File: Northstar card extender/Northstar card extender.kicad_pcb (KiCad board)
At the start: 2 copper layers, 76.1 x 36 mm, 17 parts, among them J1 male card edge, J2 female slot pass through, J3 ribbon expansion

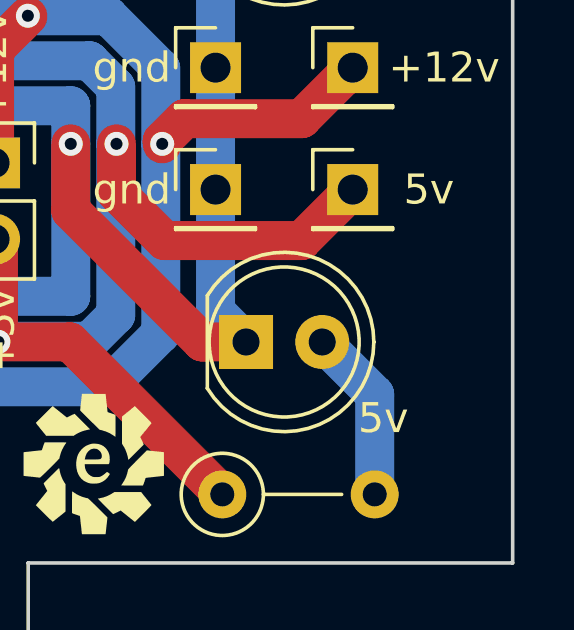
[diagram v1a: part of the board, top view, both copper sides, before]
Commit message: added silkscreen for direction
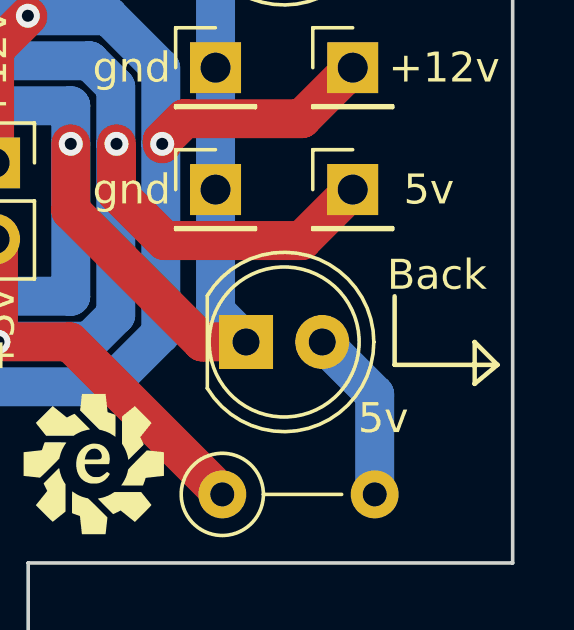
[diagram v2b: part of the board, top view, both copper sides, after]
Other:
- board text added: "Back"
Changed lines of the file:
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@@
       (stroke (width 0) (type solid)) (fill solid) (layer "B.SilkS"))
   )
+  (gr_line (start 173.482 110.744) (end 173.482 112.141)
+    (stroke (width 0.15) (type default)) (layer "F.SilkS"))
+  (gr_line (start 173.482 112.141) (end 174.244 111.506)
+    (stroke (width 0.15) (type default)) (layer "F.SilkS"))
+  (gr_line (start 174.244 111.506) (end 173.482 110.744)
+    (stroke (width 0.15) (type default)) (layer "F.SilkS"))
+  (gr_line (start 170.815 111.506) (end 174.244 111.506)
+    (stroke (width 0.15) (type default)) (layer "F.SilkS"))
+  (gr_line (start 170.815 109.22) (end 170.815 111.506)
+    (stroke (width 0.15) (type default)) (layer "F.SilkS"))
   (gr_text "/BIO RES" (at 131.318 116.078 -90) (layer "B.SilkS")
     (effects (font (size 1 1) (thickness 0.15)) (justify left bottom mirror))
@@
     (effects (font (size 1 1) (thickness 0.15)) (justify left bottom))
   )
+  (gr_text "Back" (at 170.561 109.093) (layer "F.SilkS")
+    (effects (font (size 1 1) (thickness 0.15)) (justify left bottom))
+  )
